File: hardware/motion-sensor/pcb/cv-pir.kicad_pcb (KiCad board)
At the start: 2 copper layers, 88.8 x 63.7 mm, 29 parts, among them J1 USB-C 16P, K1 SRD-05, M1 HC-SR501 PIR, Q1 S8050, U1 ESP32-WROOM-32E (4MB), U2 AMS1117-3.3, U3 PC817

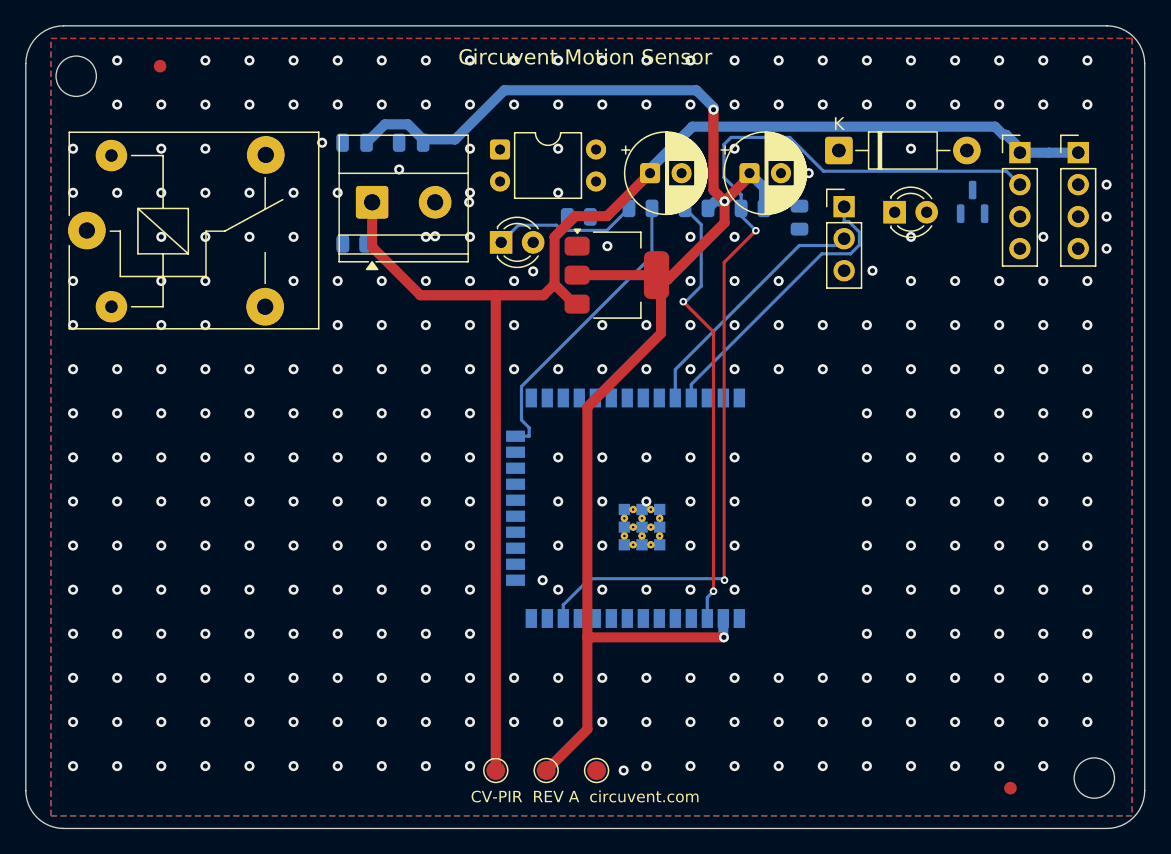
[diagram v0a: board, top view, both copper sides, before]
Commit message: hardware: fix mains isolation barrier gaps, add load-controller PCB
Adds the 13th board (ultra-compact dual-channel load controller: ESP32-C3,
opto+relay channel, MOSFET PWM channel, USB-C, AP2112K LDO, USBLC6 ESD) and
regenerates all 12 existing boards, which were stale with respect to earlier
relay-pinout and LED-polarity fixes.

The substantive change is to the mains isolation barrier. It is a keepout band
the router must not cross, deliberately cut where a component straddles it
because there the isolation is provided by the part's package. Three linked
defects made those cuts unsafe, each only visible once the previous was fixed:

1. The cut removed the barrier across the full band width for the straddling
   part's whole height, while the ISO_BRIDGE area that excuses the gap covered
   only the part itself. The router used the leftover strip beside the part to
   bring +5V within 6.99 mm of AC_N against an 8.0 mm reinforced creepage rule.
2. Straddling parts can overlap in y, so cutting per part put one part's
   keepout on another part's pads. The exempt x-ranges are now unioned per
   strip by a sweep line.
3. The rule only relaxes for items insideArea('ISO_BRIDGE'). With the hole the
   same size as the area, a track could hug the hole's edge without being
   contained in it, so the rule fired anyway and the router had no way to know.
   The hole is now the part's pad bbox + 0.3 mm, strictly inside ISO_BRIDGE at
   the footprint bbox + 0.6 mm.

The tighter hole leaves mains nets less room to reach bridge pads, so some
boards report more unconnected items. That is deliberate: those are documented
hand-routing items, whereas a creepage violation is a safety defect.

Also fixed in the generator:
- _pad_shape() derived a pad's layers from PAD::GetLayer(), which returns F.Cu
  even for pads on B.Cu. Every back-side pad became a phantom obstacle on the
  front, blocking legal paths there while hiding the real one behind. Only
  IsOnLayer() is truthful.
- Castella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
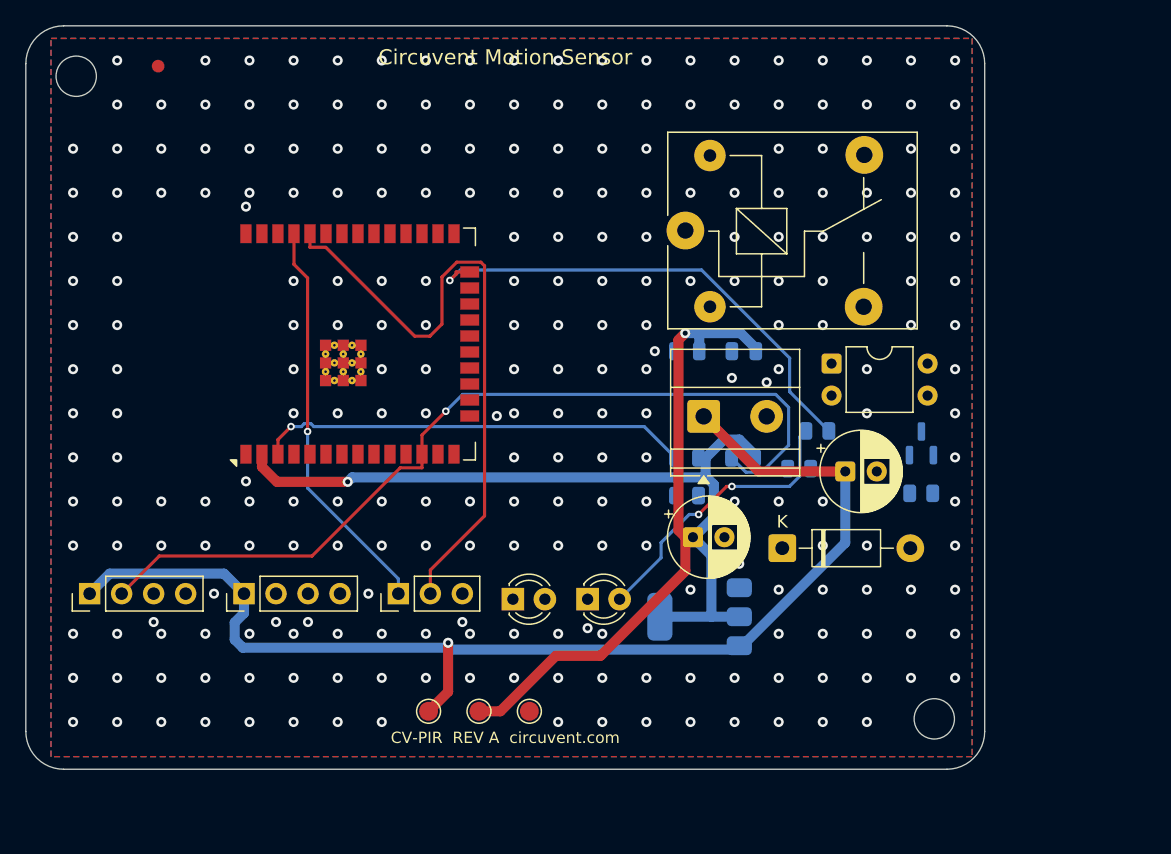
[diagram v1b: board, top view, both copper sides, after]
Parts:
- removed FID2: Fiducial, Fiducial_1mm_Mask2mm
- U1: moved to F.Cu
- U2: moved to B.Cu
- moved M1 81.7 mm to (105.1, 125.1), turned to 90 degrees
- moved BT1 74.9 mm to (117.3, 125.1), turned to 90 degrees
- moved K1 47.5 mm to (152.3, 96.2)
- moved JP 46.8 mm to (129.6, 125.1), turned to 90 degrees
- moved LED0 43.1 mm to (138.7, 125.5)
- moved R5 34.9 mm to (171.1, 117.1)
- moved R6 33.1 mm to (152.5, 117.3)
- moved D1 31.9 mm to (160.0, 121.5)
- moved U1 31.5 mm to (122.7, 105.2)
- moved U3 31.3 mm to (163.9, 106.8)
- moved J1 31.3 mm to (153.8, 111.0)
- moved C3 31.2 mm to (152.5, 105.8)
- moved C4 31.2 mm to (157.0, 105.8)
- moved C2 29.2 mm to (152.9, 120.6)
- moved LED1 29.1 mm to (144.6, 125.5)
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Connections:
- LED1 pad 1: LED_PIN_A -> GND
- LED1 pad 2: GND -> LED_PIN_A
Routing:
- net UART_RX: track 20.0 -> 50.4 mm
- net LED_PIN: track 23.7 -> 39.2 mm, vias 0 -> 1
- net +5V: track 110.5 -> 95.0 mm, vias 0 -> 1
- net LED_PIN_A: track 11.6 -> 22.8 mm, vias 0 -> 2
- net UART_TX: track 22.8 -> 32.0 mm, vias 0 -> 1
- net PIR_PIN: track 76.7 -> 70.3 mm, vias 2 -> 1
- net +3V3: track 117.3 -> 111.9 mm, vias 3 -> 2
- net EN: track 35.0 -> 34.4 mm, vias 2 -> 1
- net GND: vias 329 -> 262
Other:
- board size 88.8 x 63.7 mm -> 76.1 x 59 mm

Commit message: Release 1.10.0, and stop shipping permissions the app never uses
Cut 1.10.0 (versionCode 12) and built it: AAB 38 MB, APK 83 MB, signed with the
upload key, JS bundle embedded.

Checking the generated manifest before writing the Play listing turned up
permissions no one had asked for. Every one of them is printed on the store page
for users to read before they install:

  RECORD_AUDIO          expo-camera asks for the microphone so video can be
                        recorded with sound. This app only ever puts the camera
                        in barcode mode to read a QR label, and expo-speech is
                        output-only - it speaks, it does not listen. Left in,
                        Play lists "Microphone" against a home-control app,
                        which is alarming, unexplainable and untrue.
  SYSTEM_ALERT_WINDOW   React Native's development overlay, useless in a release
                        build and shown to users as "Display over other apps".
  READ/WRITE_EXTERNAL_STORAGE
                        Legacy storage access nothing here touches.

Stripped via android.blockedPermissions. That emits tools:node="remove", which
is a merge instruction rather than a guarantee, so it was checked against the
finished artifact with aapt2 rather than the source manifest - all four are
absent from the APK.

NEARBY_WIFI_DEVICES now carries neverForLocation. Android otherwise treats it as
location-capable, because knowing which networks are in range is enough to place
someone, and Play's data safety review treats it the same way. The app uses it
only to join a new device's setup hotspot. That flag is a promise, so the plugin
says plainly that it has to come off if scan results are ever used positionally.

What is left is defensible: location for Wi-Fi onboarding (Android requires it),
camera for the QR label, nearby-devices flagged as non-positional.

Added mobile/store/listing with the text Play asks for - title, short and full
descriptions, and what'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
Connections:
- LED0 pad 1: N$LED0.1 -> GND
- LED0 pad 2: N$LED0.2 -> LED0_A
- R3 pad 2: PIR_PIN -> LED0_A
- R4 pad 1: N$R4.1 -> +3V3
- R4 pad 2: N$R4.2 -> PIR_PIN
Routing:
- net LED0_A: track 0.00 -> 21.3 mm, vias 0 -> 1
- net UART_RX: track 50.4 -> 35.2 mm
- net +5V: track 95.0 -> 110.2 mm, vias 1 -> 0
- net UART_TX: track 32.0 -> 40.7 mm
- net +3V3: track 111.9 -> 108.7 mm, vias 2 -> 1
- net PIR_PIN: track 70.3 -> 72.9 mm
- net LED_PIN_A: track 22.8 -> 25.1 mm, vias 2 -> 1
- net LED_PIN: track 39.2 -> 39.9 mm
- net EN: track 34.4 -> 33.8 mm
- net GND: vias 262 -> 264
